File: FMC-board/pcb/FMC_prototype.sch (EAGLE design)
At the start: 80 parts, among them U1 4901, U2 TPS79333, U3 ADN4663, U4 ADN4663, U5 ADN4664, U6 PDS1-S12-S5-S, U8 4901

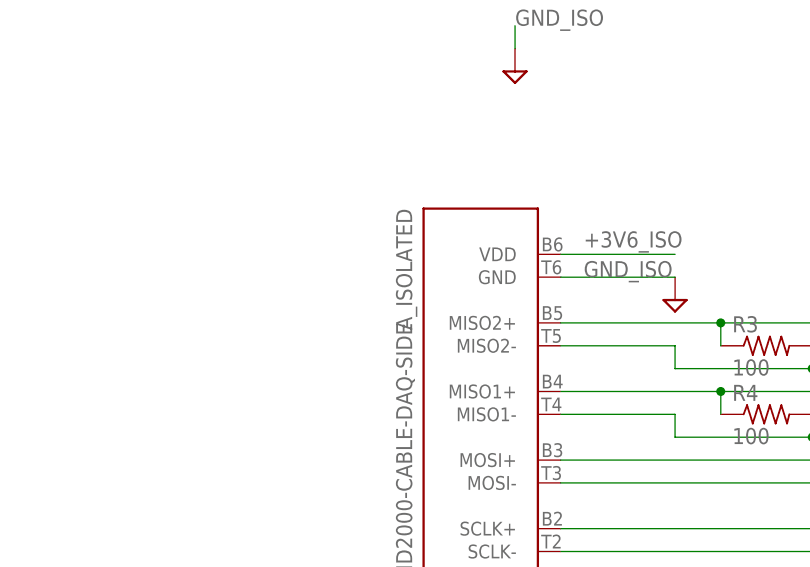
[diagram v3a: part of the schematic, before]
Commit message: some labelling
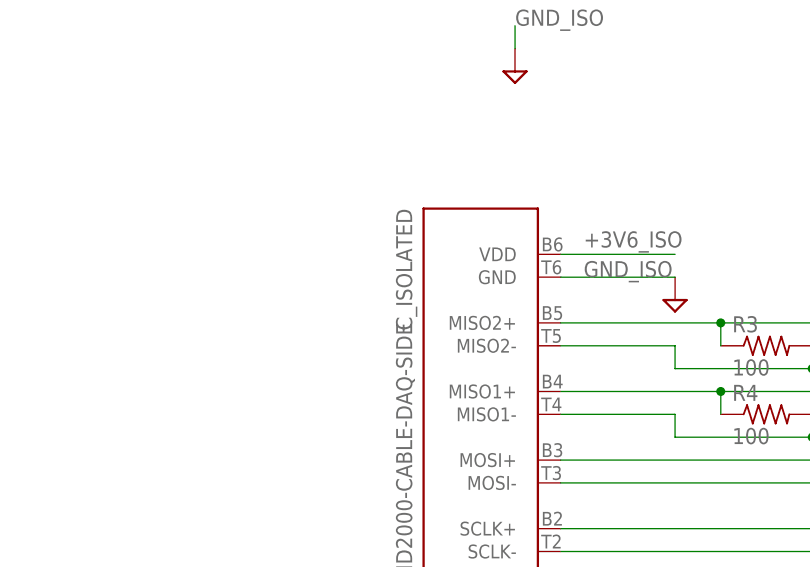
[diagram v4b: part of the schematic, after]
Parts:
- renumbered A_ISOLATED to C_ISOLATED
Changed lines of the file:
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@@
 <part name="C6" library="RHD2000_eval_board" deviceset="C" device="_0603" value="100n"/>
 <part name="C14" library="RHD2000_eval_board" deviceset="C" device="_0603" value="100n"/>
-<part name="A_ISOLATED" library="RHD2000_eval_board" deviceset="RHD2000-CABLE-DAQ-SIDE" device=""/>
+<part name="C_ISOLATED" library="RHD2000_eval_board" deviceset="RHD2000-CABLE-DAQ-SIDE" device=""/>
 <part name="R3" library="RHD2000_eval_board" deviceset="R" device="_0603" value="100"/>
 <part name="R4" library="RHD2000_eval_board" deviceset="R" device="_0603" value="100"/>
@@
 <instance part="C6" gate="C" x="170.18" y="210.82" rot="R90"/>
 <instance part="C14" gate="C" x="246.38" y="119.38" rot="R180"/>
-<instance part="A_ISOLATED" gate="A" x="88.9" y="160.02" rot="MR90"/>
+<instance part="C_ISOLATED" gate="A" x="88.9" y="160.02" rot="MR90"/>
 <instance part="R3" gate="R" x="119.38" y="170.18"/>
 <instance part="R4" gate="R" x="119.38" y="162.56"/>
@@
 <wire x1="132.08" y1="187.96" x2="132.08" y2="167.64" width="0.1524" layer="91"/>
 <wire x1="132.08" y1="167.64" x2="124.46" y2="167.64" width="0.1524" layer="91"/>
-<pinref part="A_ISOLATED" gate="A" pin="MISO2-"/>
+<pinref part="C_ISOLATED" gate="A" pin="MISO2-"/>
 <pinref part="R3" gate="R" pin="2"/>
 <wire x1="124.46" y1="167.64" x2="109.22" y2="167.64" width="0.1524" layer="91"/>
@@
 <wire x1="134.62" y1="198.12" x2="134.62" y2="165.1" width="0.1524" layer="91"/>
 <wire x1="134.62" y1="165.1" x2="114.3" y2="165.1" width="0.1524" layer="91"/>
-<pinref part="A_ISOLATED" gate="A" pin="MISO1+"/>
+<pinref part="C_ISOLATED" gate="A" pin="MISO1+"/>
 <pinref part="R4" gate="R" pin="1"/>
 <wire x1="114.3" y1="165.1" x2="96.52" y2="165.1" width="0.1524" layer="91"/>
@@
 <wire x1="137.16" y1="195.58" x2="137.16" y2="160.02" width="0.1524" layer="91"/>
 <wire x1="137.16" y1="160.02" x2="124.46" y2="160.02" width="0.1524" layer="91"/>
-<pinref part="A_ISOLATED" gate="A" pin="MISO1-"/>
+<pinref part="C_ISOLATED" gate="A" pin="MISO1-"/>
 <pinref part="R4" gate="R" pin="2"/>
 <wire x1="124.46" y1="160.02" x2="109.22" y2="160.02" width="0.1524" layer="91"/>
@@
 <wire x1="114.3" y1="172.72" x2="129.54" y2="172.72" width="0.1524" layer="91"/>
 <wire x1="129.54" y1="172.72" x2="129.54" y2="190.5" width="0.1524" layer="91"/>
-<pinref part="A_ISOLATED" gate="A" pin="MISO2+"/>
+<pinref part="C_ISOLATED" gate="A" pin="MISO2+"/>
 <pinref part="R3" gate="R" pin="1"/>
 <wire x1="114.3" y1="170.18" x2="114.3" y2="172.72" width="0.1524" layer="91"/>
@@
 <wire x1="104.14" y1="109.22" x2="104.14" y2="139.7" width="0.1524" layer="91"/>
 <pinref part="U4" gate="G$1" pin="DOUT1-"/>
-<pinref part="A_ISOLATED" gate="A" pin="!CS!-"/>
+<pinref part="C_ISOLATED" gate="A" pin="!CS!-"/>
 <wire x1="104.14" y1="139.7" x2="96.52" y2="139.7" width="0.1524" layer="91"/>
 </segment>
@@
 <net name="GND_ISO" class="0">
 <segment>
-<pinref part="A_ISOLATED" gate="A" pin="GND"/>
+<pinref part="C_ISOLATED" gate="A" pin="GND"/>
 <wire x1="109.22" y1="177.8" x2="96.52" y2="177.8" width="0.1524" layer="91"/>
 <pinref part="GND100" gate="G$1" pin="GND_ISO"/>
@@
 <wire x1="96.52" y1="180.34" x2="109.22" y2="180.34" width="0.1524" layer="91"/>
 <label x="99.06" y="182.88" size="1.778" layer="95" rot="MR180"/>
-<pinref part="A_ISOLATED" gate="A" pin="VDD"/>
+<pinref part="C_ISOLATED" gate="A" pin="VDD"/>
 </segment>
 <segment>
@@
 <net name="CS+_ISOLATED" class="0">
 <segment>
-<pinref part="A_ISOLATED" gate="A" pin="!CS!+"/>
+<pinref part="C_ISOLATED" gate="A" pin="!CS!+"/>
 <wire x1="144.78" y1="111.76" x2="106.68" y2="111.76" width="0.1524" layer="91"/>
 <pinref part="U4" gate="G$1" pin="DOUT1+"/>
@@
 <net name="N$12" class="0">
 <segment>
-<pinref part="A_ISOLATED" gate="A" pin="MOSI+"/>
+<pinref part="C_ISOLATED" gate="A" pin="MOSI+"/>
 <pinref part="U3" gate="G$1" pin="DOUT1+"/>
 <wire x1="96.52" y1="157.48" x2="144.78" y2="157.48" width="0.1524" layer="91"/>
@@
 <pinref part="U3" gate="G$1" pin="DOUT1-"/>
 <wire x1="144.78" y1="154.94" x2="96.52" y2="154.94" width="0.1524" layer="91"/>
-<pinref part="A_ISOLATED" gate="A" pin="MOSI-"/>
+<pinref part="C_ISOLATED" gate="A" pin="MOSI-"/>
 </segment>
 </net>
 <net name="N$15" class="0">
 <segment>
-<pinref part="A_ISOLATED" gate="A" pin="SCLK+"/>
+<pinref part="C_ISOLATED" gate="A" pin="SCLK+"/>
 <pinref part="U3" gate="G$1" pin="DOUT2+"/>
 <wire x1="96.52" y1="149.86" x2="144.78" y2="149.86" width="0.1524" layer="91"/>
@@
 <pinref part="U3" gate="G$1" pin="DOUT2-"/>
 <wire x1="144.78" y1="147.32" x2="96.52" y2="147.32" width="0.1524" layer="91"/>
-<pinref part="A_ISOLATED" gate="A" pin="SCLK-"/>
-</segment>
-</net>
+<pinref part="C_ISOLATED" gate="A" pin="SCLK-"/>
+</segment>
+</net>

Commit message: Overvoltage protection and silkscreen cleanup
- Finished adding Schottky protection rectifiers to all SMA inputs,
  included isolated lines.
- Left the Bezel connector floating, since this is supposed to be
  galvanically isolated from the FPGA ground. Eventually, we will
  probably tie to GND_ISO, but its more trouble than its worth now
- Cleaned up silkscreen
- Started BOM
- Added missing datasheets.
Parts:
- added D10, D11, D12, D13, D8, D9: STPS0560Z, jonnew:S-DIODESOD-123
- added R11, R12, R14: 100, jonnew:R_0603
- C17, C20, C24, C27, C29: value 100n -> 100nF
- D1, D2, D3, D5, D6, D7: value PMLL4150 -> STPS0560Z; device diode:PMLL4150 -> jonnew:S-DIODESOD-123
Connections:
- new net N$11: H23.1, R11.2
- new net N$14: H14.1, R12.2
- new net N$17: H13.1, R14.2
- net +3V3_ISO: now also D12.C, D13.C, D8.C
- net GND: no longer U$2.BEZ1, U$2.BEZ2
- net GND_ISO: now also D10.A, D11.A, D9.A
- net H13_ISO: now also D11.C, D13.A, R14.1; no longer H13.1
- net H14_ISO: now also D10.C, D12.A, R12.1; no longer H14.1
- net H23_ISO: now also D8.A, D9.C, R11.1; no longer H23.1
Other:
- moved on the sheet: G1, G2, G3, H13, H14, H23, R10, R8, R9

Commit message: More silkscreen fixes and test points
- Added test pads for digital lines on paths through isolation
  circuitry. Used small inline padsto prevent stubs.
- Silkscreen looks pretty good now.
- Boards needs a fresh look over then fab, I think.
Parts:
- removed C33: 1nF, jonnew:C_0603
- removed C34: 10uF, jonnew:C-POL_1206
- removed C40: 10uF, puggleboard:C_1206
- removed R17: 10k, jonnew:R_0603
- removed U$1: OPEN_EPHYS_LOGO, open-ephys:OPEN_EPHYS_LOGO
- removed U$2: FMC_SINGLE_WIDTH_MODULE, jonnew:FMC_SINGLE_WIDTH_MODULE
- added C19: 2.2uF, jonnew:C_1206
- added C25: 100nF, RHD2000_eval_board:C_0603
- added C26: 22uF, jonnew:C-POL_1210
- added PWR_ISO: 569-011x, jonnew:LED_2X_VERTICAL
- added R15: 100, jonnew:R_0603
- added TP1: GND-ISO, jonnew:TPTP06R
- added TP10: SCLK-, jonnew:TPTP06R
- added TP11: CS+, jonnew:TPTP06R
- added TP12: CS-, jonnew:TPTP06R
- added TP3: MISO2+, jonnew:TPTP06R
- added TP4: MISO2-, jonnew:TPTP06R
- added TP5: MISO1+, jonnew:TPTP06R
- added TP6: MISO1-, jonnew:TPTP06R
- added TP7: MOSI+, jonnew:TPTP06R
- added TP8: MOSI-, jonnew:TPTP06R
- added TP9: SCLK+, jonnew:TPTP06R
- added TP_CS: CS, jonnew:TPTP06R
- added TP_H13: H13, jonnew:TPTP06R
- added TP_H14: H14, jonnew:TPTP06R
- added TP_H23: H23, jonnew:TPTP06R
- added TP_MISO1: MISO1, jonnew:TPTP06R
- added TP_MISO2: MISO2, jonnew:TPTP06R
- added TP_MOSI: MOSI, jonnew:TPTP06R
- added TP_SCLK: SCLK, jonnew:TPTP06R
- added U7: 4901, puggleboard:TPS7A4901DGNR
- C10: value 1.0u -> 100nF; device RHD2000_eval_board:C_0805 -> RHD2000_eval_board:C_0603
- C11: value 10uF -> 1nF; device jonnew:C_1206 -> jonnew:C_0603
- C12: value 100n -> 10uF; device RHD2000_eval_board:C_0603 -> puggleboard:C_1206
- C13: value 100n -> 1.0uF; device RHD2000_eval_board:C_0603 -> RHD2000_eval_board:C_0805
- C14: value 100n -> 10uF; device RHD2000_eval_board:C_0603 -> jonnew:C_1206
- C15, C8: value 100n -> 100nF
- C16: value 1nF -> 100nF; device jonnew:C_0603 -> RHD2000_eval_board:C_0603
- C18: value 2.2uF -> 100nF; device jonnew:C_1206 -> RHD2000_eval_board:C_0603
- C2: value 10uF -> 10nF; device puggleboard:C_1206 -> jonnew:C_0603
- C20, C24: value 100nF -> 10uF; device RHD2000_eval_board:C_0603 -> puggleboard:C_1206
- C21: value 10uF -> 1nF; device puggleboard:C_1206 -> jonnew:C_0603
- C28: value 100n -> 22uF; device RHD2000_eval_board:C_0603 -> jonnew:C-POL_1210
- C3: value 22u -> 22uF
- C30, C31: value 22uF -> 100nF; device jonnew:C-POL_1210 -> RHD2000_eval_board:C_0603
- C32: value 10uF -> 100nF; device jonnew:C-POL_1206 -> RHD2000_eval_board:C_0603
- C4: value 10nF -> 10uF; device jonnew:C_0603 -> jonnew:C-POL_1206
- C5: value 10n -> 10uF; device RHD2000_eval_board:C_0603 -> jonnew:C-POL_1206
- C6: value 100n -> 10nF
- C7: value 100n -> 10nF; device RHD2000_eval_board:C_0603 -> jonnew:C_0603
- C9: value 10nF -> 100nF; device jonnew:C_0603 -> RHD2000_eval_board:C_0603
- D4: value 8V -> STPS0560Z; device jonnew:Z-DIODE_SOD-323 -> jonnew:S-DIODESOD-123
- D7: value STPS0560Z -> BZT52C7V5; device jonnew:S-DIODESOD-123 -> jonnew:Z-DIODE_SOD123
- DO_ISO: value IS07640 -> ISO7640
- H13, H14, H23: value 142-0701 -> SMA002
- R1, R16: value 20k -> 100
- R10, R11: value 100 -> 10k
- R12: value 100 -> 20k
- R13, R3: device RHD2000_eval_board:R_0603 -> jonnew:R_0603
- R2: value 820 -> 100; device RHD2000_eval_board:R_0603 -> jonnew:R_0603
- R4: value 100 -> 820
- R5: value 10k -> 20k
- R6: value 820 -> 10k; device RHD2000_eval_board:R_0603 -> jonnew:R_0603
- R7: value 10k -> 820
- R8, R9: device jonnew:R_0603 -> RHD2000_eval_board:R_0603
- U$3: value (none) -> OPEN_EPHYS_LOGO; device jonnew:LED_2X_VERTICAL -> open-ephys:OPEN_EPHYS_LOGO
- U2: value TPS79333 -> 7933
- U6: value PDS1-S12-S5-S -> PDS1
- U8: value 4901 -> FMC_SINGLE_WIDTH_MODULE; device puggleboard:TPS7A4901DGNR -> jonnew:FMC_SINGLE_WIDTH_MODULE
- renumbered C35 to C22, C37 to C23, C_ISOLATED to C_ISO, G1 to G21, G2 to G22, G3 to G24, U$4 to Q1
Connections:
- removed net C10: FMCG$1.P$130
- removed net C11: FMCG$1.P$131
- removed net C14: FMCG$1.P$134
- removed net C18: FMCG$1.P$138
- removed net N$9: FMCG$1.P$76
- removed net TP7: FMCG$1.P$135
- net +3V3: now also C18.2, C25.2, C29.2, C31.2, D10.C, D12.C, D8.C; no longer C14.2, C15.2, C20.2, C24.2, D2.C, D6.C, D7.C
- net +3V3_ISO: now also C10.1, C15.2, C16.2, C4.+, C5.+, C9.1, D1.C, D3.C, D5.C, R7.1; no longer C12.2, C13.2, C32.+, C34.+, C6.1, C7.1, D12.C, D13.C, D8.C, R2.1
- net +3V6: now also C24.1, R12.1, U7.OUT; no longer C40.1, R16.1, U8.OUT
- net +3V6_ISO: now also C1.1, R4.1, R5.1; no longer C4.1, R1.1, R6.1
- net +5V0_ISO: now also C11.1, C12.1, C13.1; no longer C1.1, C10.1, C16.1
- net +5V0_ISO-PRE: now also C14.1; no longer C11.1
- net 12V_FPGA: now also C19.1, C26.+, C28.+, C30.2, C32.2; no longer C18.1, C28.2, C29.2, C30.+, C31.+
- net AGND1: now also R12.2, R13.1, U7.FB; no longer R16.2, R17.1, U8.FB
- net AGND2: now also C2.2, R5.2, R6.1; no longer C4.2, R1.2, R5.1
- net CS: now also TP_CS.TP
- net CS+_ISOLATED: now also TP11.TP
- net CS-_ISOLATED: now also TP12.TP
- net G21: now also D8.A, D9.C, R16.1; no longer D1.C, D2.A, R8.1
- net G22: now also D10.A, D11.C, R14.1; no longer D3.C, D6.A, R9.1
- net G24: now also D12.A, D13.C, R15.1; no longer D5.C, D7.A, R10.1
- net GND: now also C18.1, C19.2, C20.2, C24.2, C25.1, C26.-, C28.-, C30.1, C31.1, C32.1, D11.A, D13.A, D9.A, R11.1, R13.2, U7.EP, U7.GND; no longer C14.1, C15.1, C18.2, C20.1, C24.1, C28.1, C30.-, C31.-, C33.2, C40.2, D1.A, D3.A, D5.A, R13.1, R17.2, U8.EP, U8.GND
- net GND_ISO: now also C12.2, C13.2, C14.2, C15.1, C16.1, C4.-, C5.-, D2.A, D4.A, D6.A, PWR_ISO1.C, PWR_ISO2.C, R10.1, R6.2, TP1.TP; no longer C12.1, C13.1, C16.2, C2.2, C32.-, C34.-, C5.2, D10.A, D11.A, D9.A, R5.2, R7.1, U$31.C, U$32.C
- net H13: now also TP_H13.TP
- net H13_ISO: now also D5.A, D6.C, R3.1; no longer D11.C, D13.A, R14.1
- net H14: now also TP_H14.TP
- net H14_ISO: now also D3.A, D4.C, R2.1; no longer D10.C, D12.A, R12.1
- net H23: now also TP_H23.TP
- net H23_ISO: now also D1.A, D2.C, R1.1; no longer D8.A, D9.C, R11.1
- net MISO1: now also TP_MISO1.TP
- net MISO1+_ISOLATED: now also R9.1, TP5.TP; no longer R4.1
- net MISO1-_ISOLATED: now also R9.2, TP6.TP; no longer R4.2
- net MISO2: now also TP_MISO2.TP
- net MISO2+_ISOLATED: now also R8.1, TP3.TP; no longer R3.1
- net MISO2-_ISOLATED: now also R8.2, TP4.TP; no longer R3.2
- net MOSI: now also TP_MOSI.TP
- net N$1: now also U7.NR/SS; no longer U8.NR/SS
- net N$10: now also PWR_ISO1.A, R7.2; no longer R2.2, U$31.A
- net N$11: now also R1.2; no longer R11.2
- net N$12: now also TP7.TP
- net N$13: now also TP8.TP
- net N$14: now also R2.2; no longer R12.2
- net N$15: now also TP9.TP
- net N$16: now also TP10.TP
- net N$17: now also R3.2; no longer R14.2
- net N$18: now also R14.2; no longer R9.2
- net N$19: now also R15.2; no longer R10.2
- net N$2: now also R16.2; no longer R8.2
- net N$3: now also D7.C; no longer D4.C
- net N$4: now also C7.1; no longer C9.1
- net N$5: now also R10.2; no longer R7.2
- net N$6: now also D7.A, R11.2; no longer D4.A, R13.2
- net N$8: now also PWR_ISO2.A, R4.2; no longer R6.2, U$32.A
- net N$97: now also C6.1; no longer C5.1
- net SCLK: now also TP_SCLK.TP
- net VDD_POST_LC: now also C20.1, U7.EN, U7.IN; no longer C33.1, U8.EN, U8.IN
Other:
- moved on the sheet: C1, C10, C11, C12, C13, C14, C15, C16, C17, C18, C2, C20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

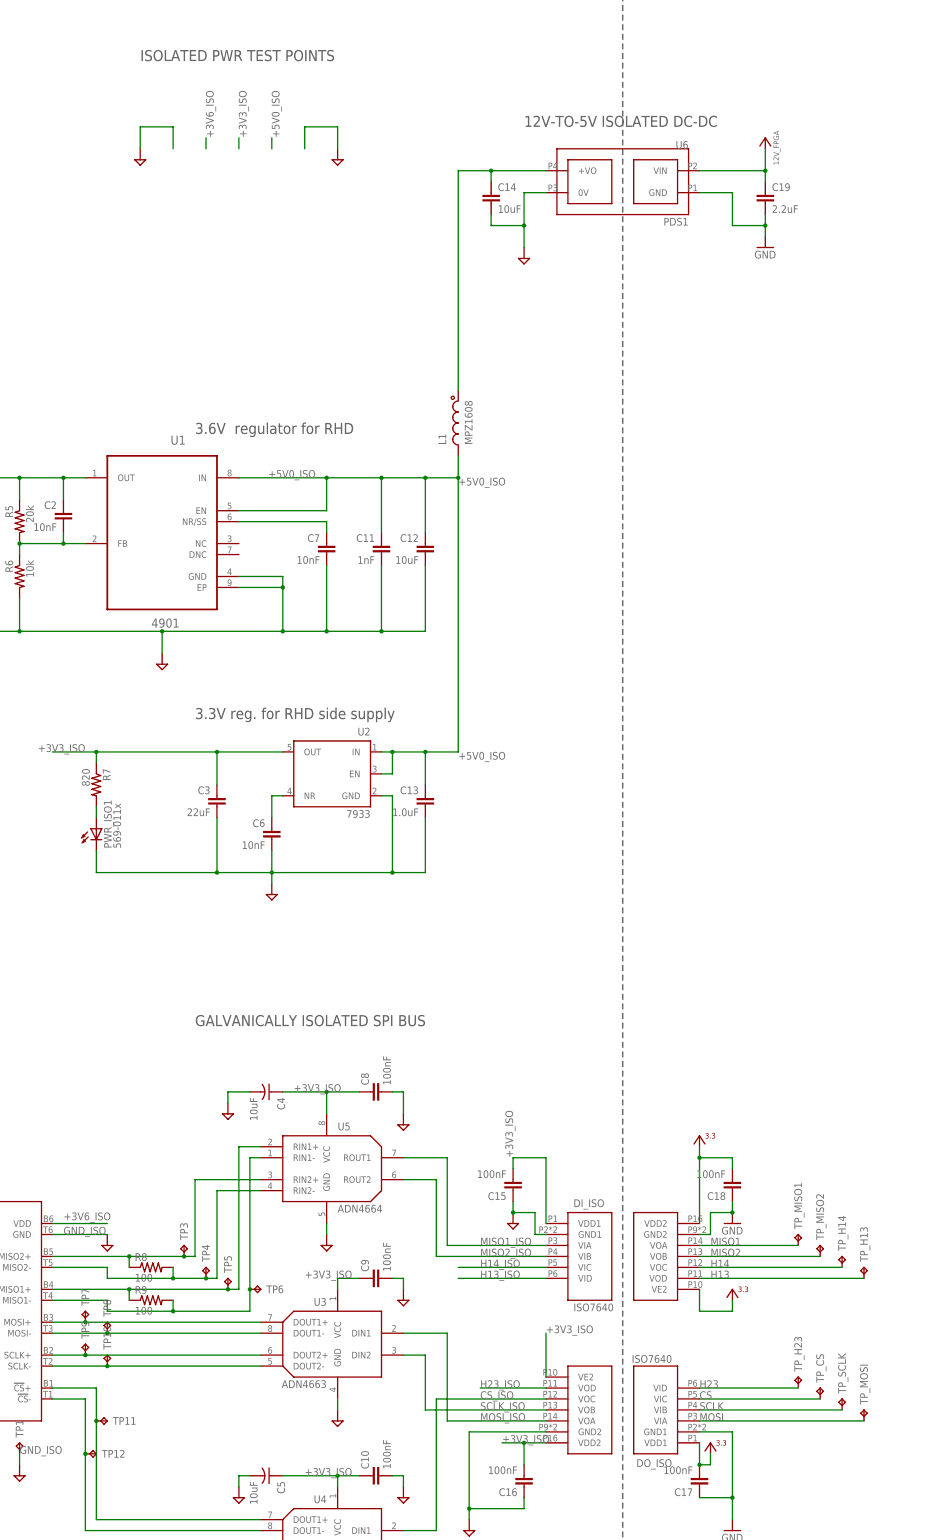
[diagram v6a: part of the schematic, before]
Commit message: Final, minor changes to sinkscreen and tp's
- Added isolated power test points
- Moved Jakobs annotations to the tplace and bplace layers, so that they
  will be included in the silkscreen using the CAM job I added
- Added a well-tested CAM job for 4-layer boards
- Added resultant gerber files for PCB and stencil
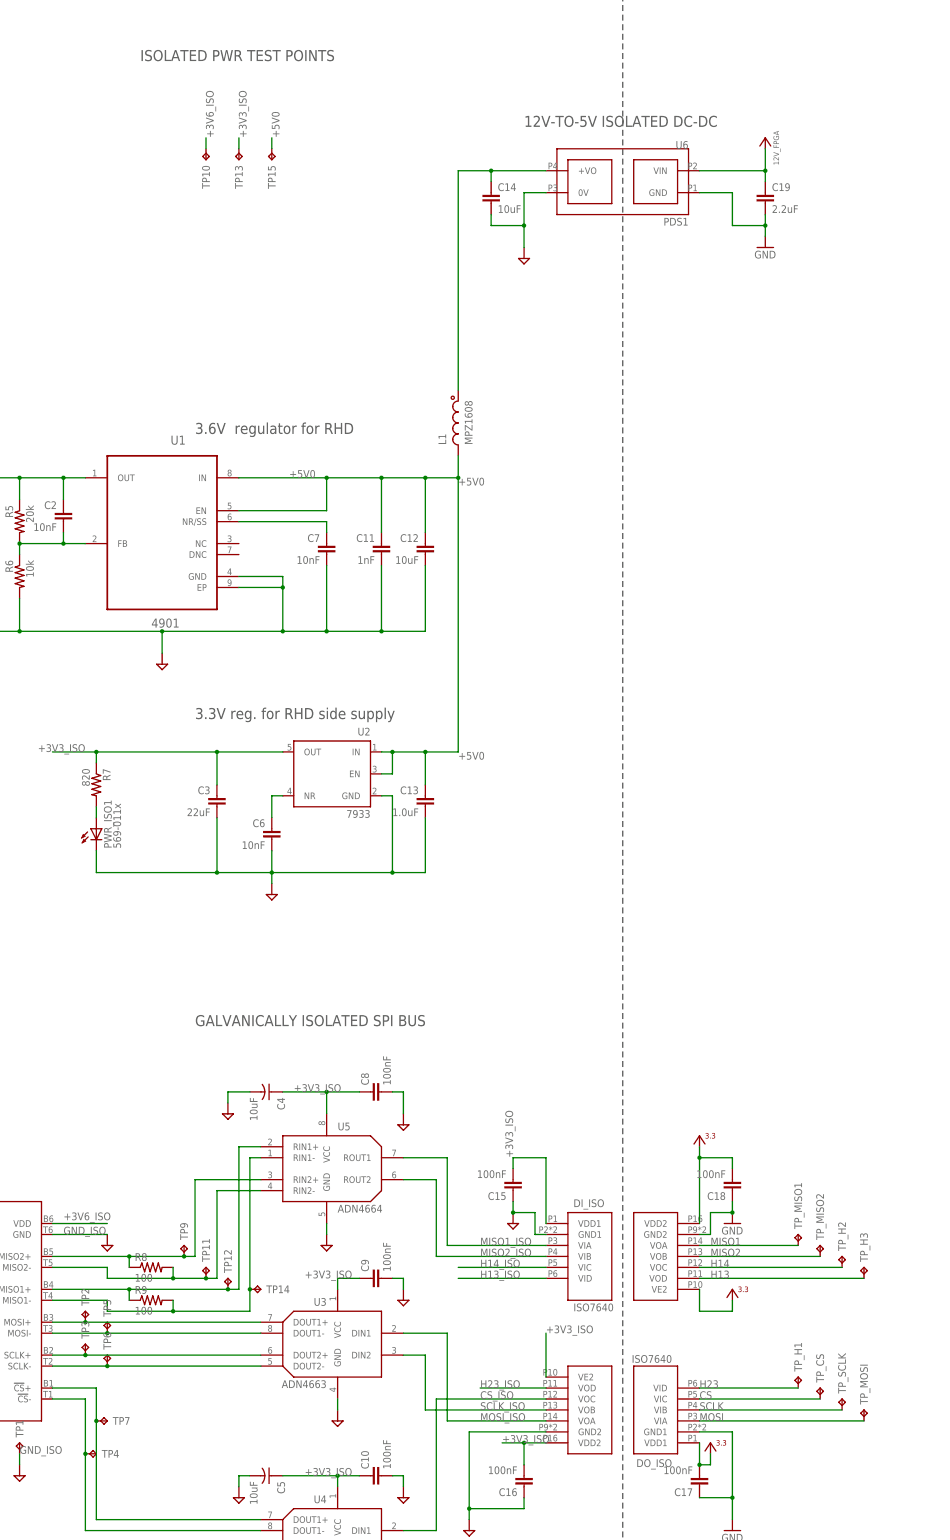
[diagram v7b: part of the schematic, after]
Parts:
- removed TP8: MOSI-, jonnew:TPTP06R
- added TP13: +3V3, jonnew:TPTP06R
- added TP14: MISO1-, jonnew:TPTP06R
- added TP15: +5V0, jonnew:TPTP06R
- added TP2: MOSI+, jonnew:TPTP06R
- TP1: device jonnew:TPTP06R -> jonnew:TPPAD1-13
- TP10: value SCLK- -> +3V6
- TP11: value CS+ -> MISO2-
- TP12: value CS- -> MISO1+
- TP3: value MISO2+ -> SCLK+
- TP4: value MISO2- -> CS-
- TP5: value MISO1+ -> MOSI-
- TP6: value MISO1- -> SCLK-
- TP7: value MOSI+ -> CS+
- TP9: value SCLK+ -> MISO2+
- renumbered TP_H13 to TP_H3, TP_H14 to TP_H2, TP_H23 to TP_H1, U$3 to U$1
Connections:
- removed net +5V0_ISO: C11.1, C12.1, C13.1, L1.2, U1.EN, U1.IN, U2.EN, U2.IN
- new net +5V0: C11.1, C12.1, C13.1, L1.2, TP15.TP, U1.EN, U1.IN, U2.EN, U2.IN
- net +3V3_ISO: now also TP13.TP
- net +3V6_ISO: now also TP10.TP
- net CS+_ISOLATED: now also TP7.TP; no longer TP11.TP
- net CS-_ISOLATED: now also TP4.TP; no longer TP12.TP
- net MISO1+_ISOLATED: now also TP12.TP; no longer TP5.TP
- net MISO1-_ISOLATED: now also TP14.TP; no longer TP6.TP
- net MISO2+_ISOLATED: now also TP9.TP; no longer TP3.TP
- net MISO2-_ISOLATED: now also TP11.TP; no longer TP4.TP
- net N$12: now also TP2.TP; no longer TP7.TP
- net N$13: now also TP5.TP; no longer TP8.TP
- net N$15: now also TP3.TP; no longer TP9.TP
- net N$16: now also TP6.TP; no longer TP10.TP
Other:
- moved on the sheet: TP10, TP11, TP12, TP3, TP4, TP5, TP6, TP7, TP9
